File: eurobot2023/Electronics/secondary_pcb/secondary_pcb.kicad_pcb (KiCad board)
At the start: 2 copper layers, 74 x 88 mm, 35 parts, among them IC1 CD74HCT125M96, IC2 SN74LVC126ADR, J1 PI40HAT, J2 Conn_01x02_Male, J3 Conn_01x02_Male, J4 Conn_01x02_Male, J5 Conn_01x02_Male, J6 Conn_01x02_Male, P1 P1, P2 Amazon 5A stepdown, U1 MCP2515-xSO, U2 TJA1049T, U4 Pololu_MAX14870

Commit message: Minor PCB fixups.
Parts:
- moved J6 5.00 mm to (135.3, 133.0), turned to -90 degrees
- moved R3 2.57 mm to (101.5, 128.8), turned to 90 degrees
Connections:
- J1 pad 33: /GPIO 13 -> unconnected-(J1-Pad33)
- J1 pad 35: /GPIO 19 -> unconnected-(J1-Pad35)
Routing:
- net /GPIO 4: track 45.1 -> 42.0 mm
- net +24V: track 58.9 -> 56.1 mm
- net Net-(C2-Pad2): track 22.7 -> 20.2 mm
- net /GPIO 21: track 29.6 -> 27.4 mm
- net /SPI1 CLK_5: track 42.5 -> 40.6 mm
- net +3.3V: track 183.4 -> 181.9 mm, vias 2 -> 4
- net Net-(Enc1-Pad4): track 66.4 -> 65.1 mm
- net /GPIO 17: track 40.0 -> 38.7 mm, vias 4 -> 2
- net /GPIO 20: track 23.7 -> 24.9 mm
- net Net-(CAN1-Pad2): track 90.2 -> 89.1 mm
- net /SPI1 MOSI_5: track 46.4 -> 45.7 mm
- net Net-(CAN1-Pad1): track 86.6 -> 86.0 mm
- net /I2C SCL: track 112.0 -> 111.4 mm, vias 2 -> 4
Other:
- board text added: "17"
- board text added: "27"
- board text removed: "13"
- board text removed: "19"

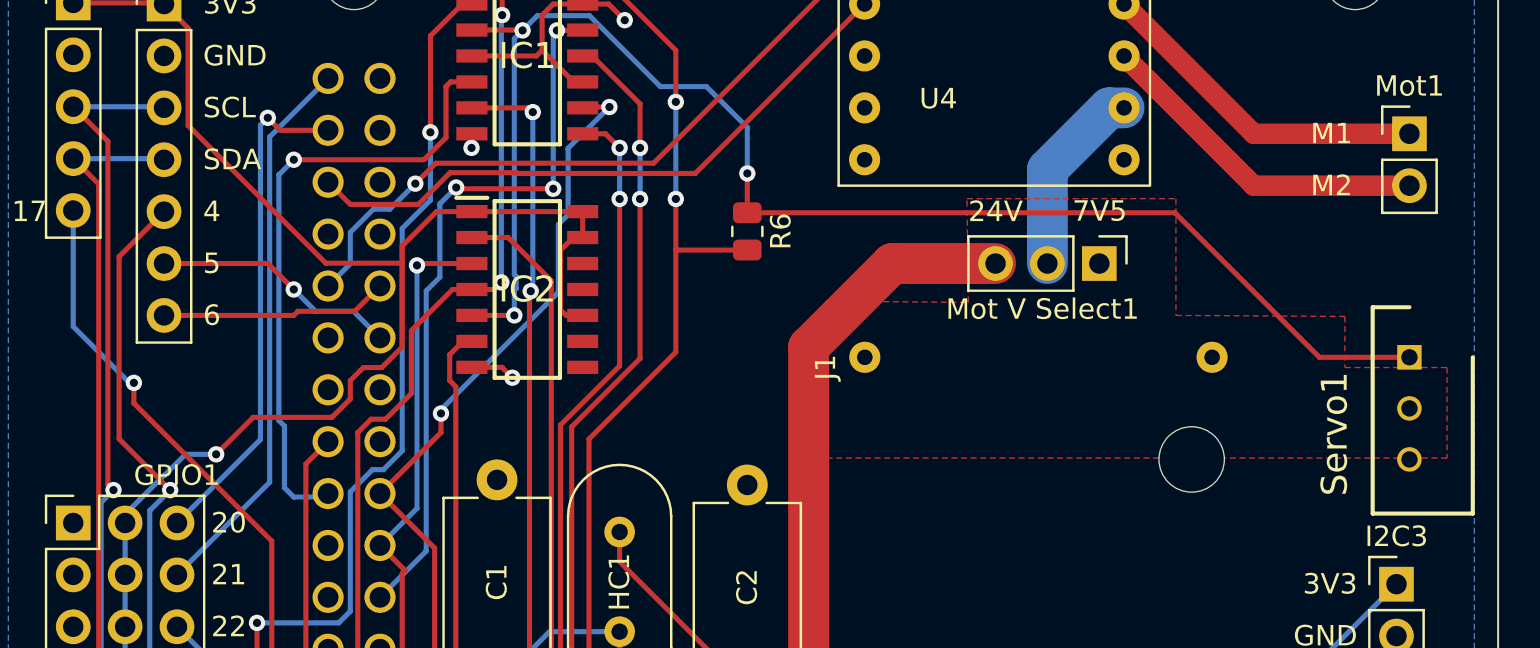
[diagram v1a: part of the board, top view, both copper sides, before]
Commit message: Rework logger mechanism to make it more powerfull  - allow logging of arbitrary variables declared on the fly  - rely on HDF5 for long-term support  - use Teleplot for live debug
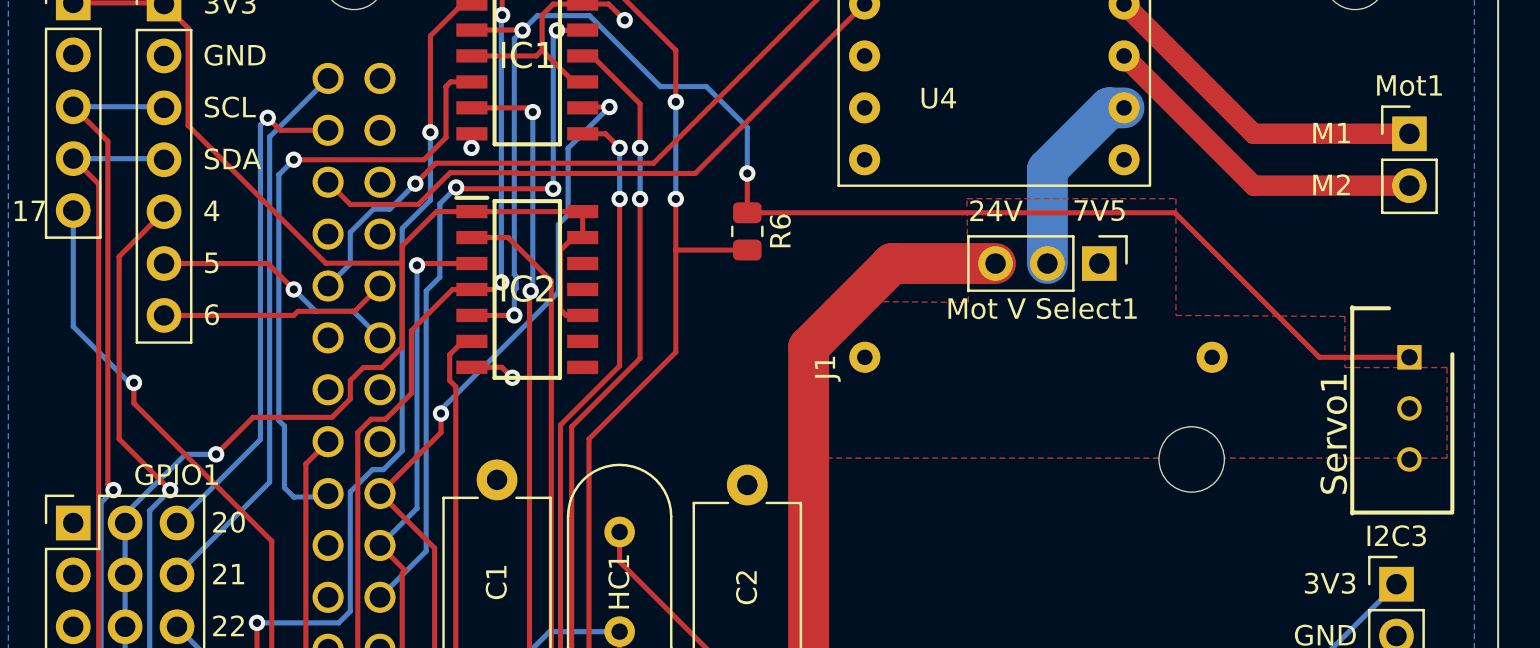
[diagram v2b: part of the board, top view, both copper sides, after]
